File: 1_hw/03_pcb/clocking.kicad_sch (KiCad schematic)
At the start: 0 parts

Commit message: FEAT: Swapped out DDS IC and connected. Started adding Clockign Components into Schematic.
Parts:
- added U?: ADG1219BRJZ, TBD, symbol BRZK_MUX:ADG1219BRJZ
- added X?: ASE-10.000MHz, Oscillator:Oscillator_SMD_Abracon_ASE-4Pin_3.2x2.5mm, symbol Oscillator:ASE-xxxMHz
- added X?: ASE-100.000MHz, Oscillator:Oscillator_SMD_Abracon_ASE-4Pin_3.2x2.5mm, symbol Oscillator:ASE-xxxMHz
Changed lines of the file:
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@@
 		(company "Tomasz Brzyzek")
 	)
+	(symbol
+		(lib_id "Oscillator:ASE-xxxMHz")
+		(at 97.79 72.39 0)
+		(unit 1)
+		(exclude_from_sim no)
+		(in_bom yes)
+		(on_board yes)
+		(dnp no)
+		(property "Reference" "X?"
+			(at 111.76 66.04 0)
+			(effects
+				(font
+					(size 1.27 1.27)
+				)
+			)
+		)
+		(property "Value" "ASE-10.000MHz"
+			(at 111.76 68.58 0)
+			(effects
+				(font
+					(size 1.27 1.27)
+				)
+			)
+		)
+		(property "Footprint" "Oscillator:Oscillator_SMD_Abracon_ASE-4Pin_3.2x2.5mm"
+			(at 115.57 81.28 0)
+			(effects
+				(font
+					(size 1.27 1.27)
+				)
+				(hide yes)
+			)
+		)
+		(property "Datasheet" "http://www.abracon.com/Oscillators/ASV.pdf"
+			(at 95.25 72.39 0)
+			(effects
+				(font
+					(size 1.27 1.27)
+				)
+				(hide yes)
+			)
+		)
+		(property "Description" "3.3V CMOS SMD Crystal Clock Oscillator, Abracon"
+			(at 97.79 72.39 0)
+			(effects
+				(font
+					(size 1.27 1.27)
+				)
+				(hide yes)
+			)
+		)
+		(pin "2"
+		)
+		(pin "3"
+		)
+		(pin "1"
+		)
+		(pin "4"
+		)
+		(instances
+			(project ""
+				(path "/866ef9be-3b01-4288-a6e0-a2357aa17e50/59503b16-13c4-4480-8e22-c5a7043d8844"
+					(reference "X?")
+					(unit 1)
+				)
+			)
+		)
+	)
+	(symbol
+		(lib_id "BRZK_MUX:ADG1219BRJZ")
+		(at 58.42 100.33 0)
+		(mirror y)
+		(unit 1)
+		(exclude_from_sim no)
+		(in_bom yes)
+		(on_board yes)
+		(dnp no)
+		(fields_autoplaced yes)
+		(property "Reference" "U?"
+			(at 40.64 94.0114 0)
+			(effects
+				(font
+					(size 1.27 1.27)
+				)
+			)
+		)
+		(property "Value" "ADG1219BRJZ"
+			(at 40.64 96.5514 0)
+			(effects
+				(font
+					(size 1.27 1.27)
+				)
+			)
+		)
+		(property "Footprint" "TBD"
+			(at 58.42 102.87 0)
+			(effects
+				(font
+					(size 1.27 1.27)
+				)
+				(hide yes)
+			)
+		)
+		(property "Datasheet" "https://www.analog.com/media/en/technical-documentation/data-sheets/ADG1219.pdf"
+			(at 58.42 100.33 0)
+			(effects
+				(font
+					(size 1.27 1.27)
+				)
+				(hide yes)
+			)
+		)
+		(property "Description" "Low Capacitance, Low Charge Injection, ±15 V/12 V iCMOS® SPDT in SOT-23"
+			(at 58.42 100.33 0)
+			(effects
+				(font
+					(size 1.27 1.27)
+				)
+				(hide yes)
+			)
+		)
+		(pin "6"
+		)
+		(pin "5"
+		)
+		(pin "4"
+		)
+		(pin "3"
+		)
+		(pin "8"
+		)
+		(pin "7"
+		)
+		(pin "2"
+		)
+		(pin "1"
+		)
+		(instances
+			(project "arb"
+				(path "/866ef9be-3b01-4288-a6e0-a2357aa17e50/59503b16-13c4-4480-8e22-c5a7043d8844"
+					(reference "U?")
+					(unit 1)
+				)
+			)
+		)
+	)
+	(symbol
+		(lib_id "Oscillator:ASE-xxxMHz")
+		(at 90.17 148.59 0)
+		(unit 1)
+		(exclude_from_sim no)
+		(in_bom yes)
+		(on_board yes)
+		(dnp no)
+		(property "Reference" "X?"
+			(at 104.14 142.24 0)
+			(effects
+				(font
+					(size 1.27 1.27)
+				)
+			)
+		)
+		(property "Value" "ASE-100.000MHz"
+			(at 104.14 144.78 0)
+			(effects
+				(font
+					(size 1.27 1.27)
+				)
+			)
+		)
+		(property "Footprint" "Oscillator:Oscillator_SMD_Abracon_ASE-4Pin_3.2x2.5mm"
+			(at 107.95 157.48 0)
+			(effects
+				(font
+					(size 1.27 1.27)
+				)
+				(hide yes)
+			)
+		)
+		(property "Datasheet" "http://www.abracon.com/Oscillators/ASV.pdf"
+			(at 87.63 148.59 0)
+			(effects
+				(font
+					(size 1.27 1.27)
+				)
+				(hide yes)
+			)
+		)
+		(property "Description" "3.3V CMOS SMD Crystal Clock Oscillator, Abracon"
+			(at 90.17 148.59 0)
+			(effects
+				(font
+					(size 1.27 1.27)
+				)
+				(hide yes)
+			)
+		)
+		(pin "2"
+		)
+		(pin "3"
+		)
+		(pin "1"
+		)
+		(pin "4"
+		)
+		(instances
+			(project "arb"
+				(path "/866ef9be-3b01-4288-a6e0-a2357aa17e50/59503b16-13c4-4480-8e22-c5a7043d8844"
+					(reference "X?")
+					(unit 1)
+				)
+			)
+		)
+	)
 )

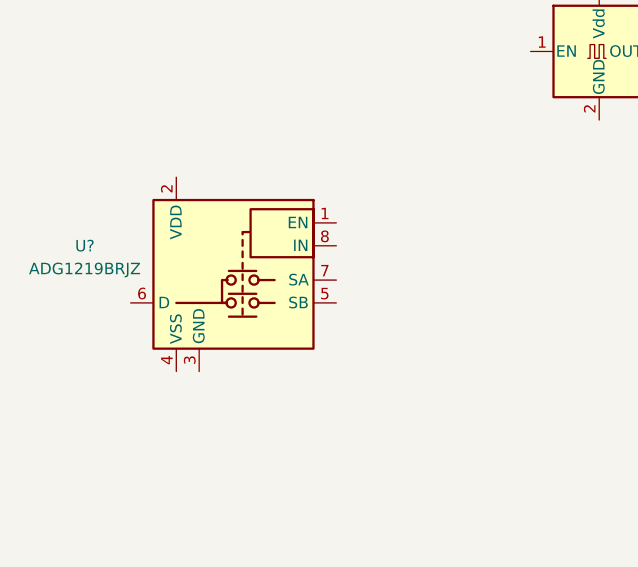
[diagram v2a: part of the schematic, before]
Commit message: FEAT: Added +15V and -15V Regulator. Replaced some Symbols to add additional Part Number Field.
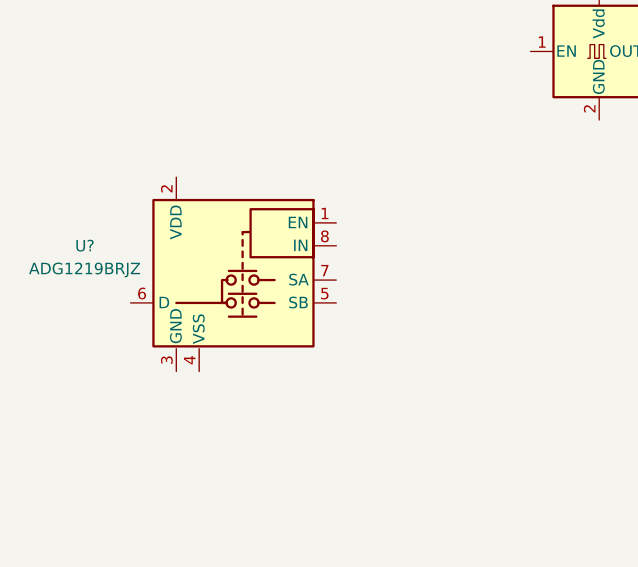
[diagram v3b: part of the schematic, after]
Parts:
- U?: footprint TBD -> BRZK_TBD; Part Number (none) -> ADG1219BRJZ
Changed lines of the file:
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@@
 			)
 		)
-		(property "Footprint" "TBD"
+		(property "Footprint" "BRZK_TBD"
 			(at 58.42 102.87 0)
 			(effects
@@
 			(at 58.42 100.33 0)
 			(effects
+				(font
+					(size 1.27 1.27)
+				)
+				(hide yes)
+			)
+		)
+		(property "Part Number" "ADG1219BRJZ"
+			(at 58.42 100.33 0)
+			(effects

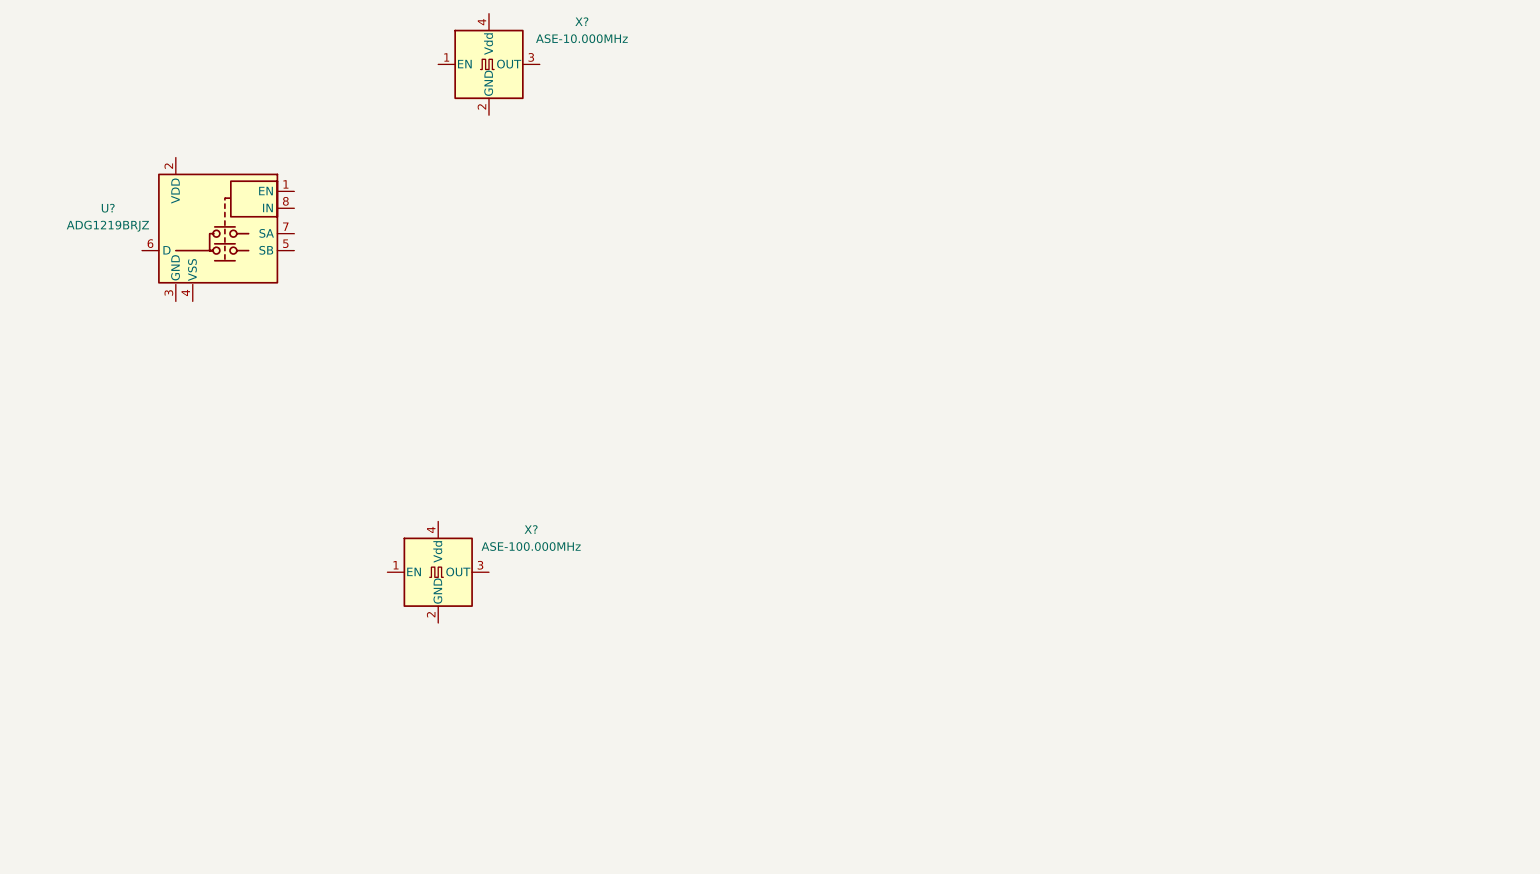
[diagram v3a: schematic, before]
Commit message: FEAT: Added Clocking Sheet, FPGA Flash, and FPGA Decoupling.
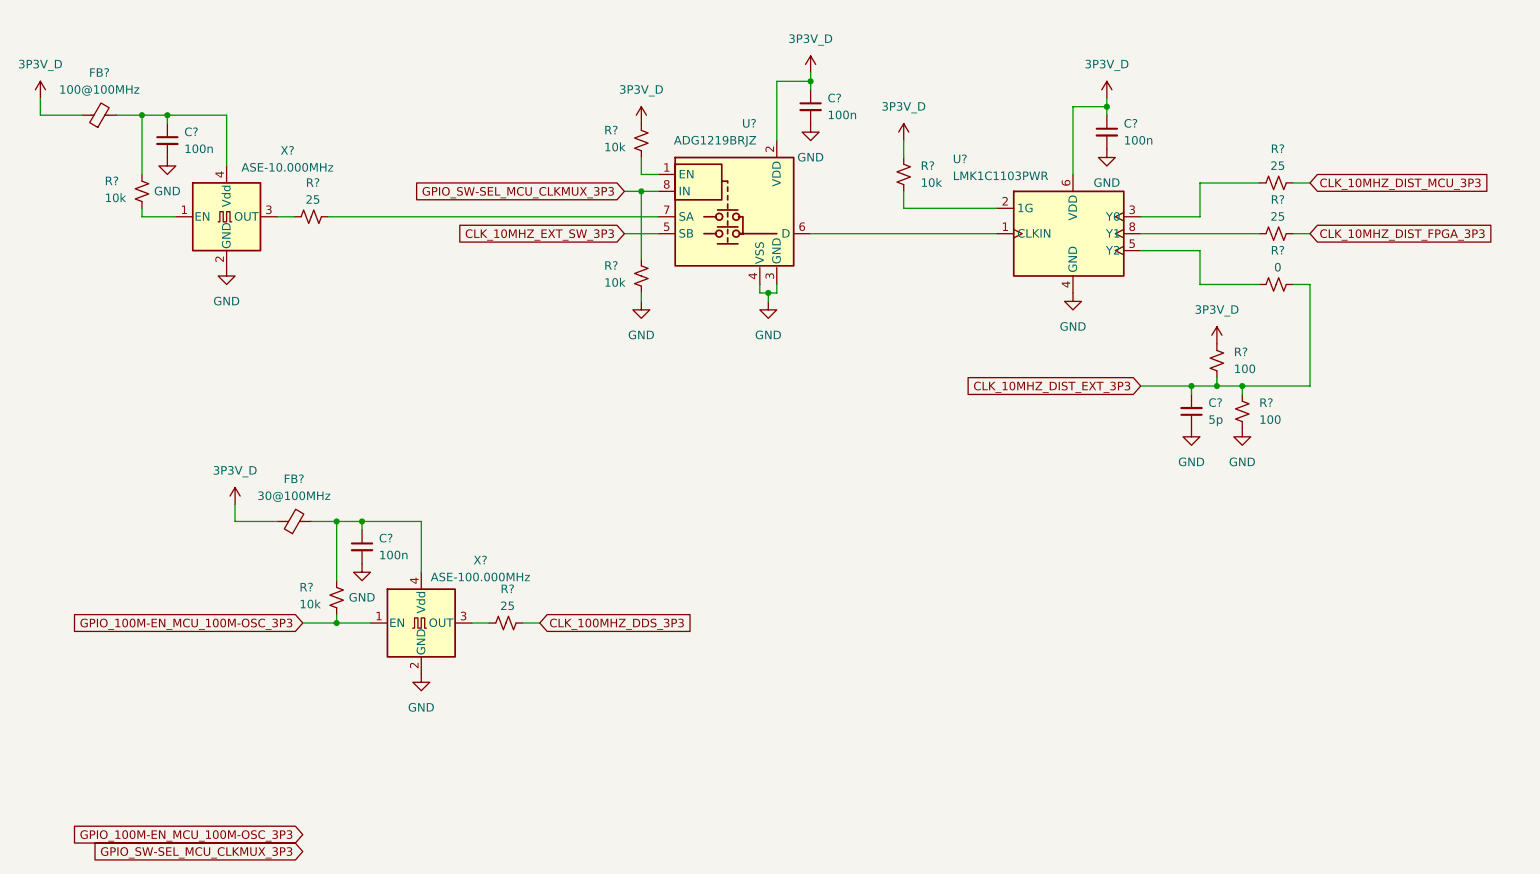
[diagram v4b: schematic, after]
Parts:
- removed X?: ASE-100.000MHz, Oscillator:Oscillator_SMD_Abracon_ASE-4Pin_3.2x2.5mm, symbol Oscillator:ASE-xxxMHz
- added C? (x4): 100n, Capacitor_SMD:C_0603_1608Metric, symbol Device:C_Small
- added C?: 5p, symbol Device:C_Small
- added FB?: 100@100MHz, symbol Device:FerriteBead_Small
- added FB?: 30@100MHz, symbol Device:FerriteBead_Small
- added R? (x4): 25, Resistor_SMD:R_0603_1608Metric, symbol Device:R_Small_US
- added R? (x5): 10k, Resistor_SMD:R_0603_1608Metric, symbol Device:R_Small_US
- added R? (x2): 100, symbol Device:R_Small_US
- added R?: 0, Resistor_SMD:R_0603_1608Metric, symbol Device:R_Small_US
- added U?: LMK1C1103PWR, Package_SO:TSSOP-8_4.4x3mm_P0.65mm, symbol BRZK_CLOCK:LMK1C1103PWR
- added X?: ASE-100.000MHz, Oscillator:Oscillator_SMD_Abracon_ASE-4Pin_3.2x2.5mm, symbol Oscillator:ASE-xxxMHz
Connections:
- net at X?.1 (EN): now also R?.1
- net GND: now reaches X?.2 (GND)
- net GND: now also U?.3 (GND), U?.4 (VSS), C?.1, C?.2, C?.2, C?.2, C?.2, R?.1, R?.1, U?.4 (GND), X?.2 (GND)
- net at X?.3 (OUT): now also R?.2
- net at X?.4 (Vdd): now also C?.1, FB?.2, R?.2
- net at U?.1 (EN): now also R?.1
- net 3P3V_D: now reaches U?.2 (VDD)
- net 3P3V_D: now also C?.1, C?.1, FB?.1, FB?.1, R?.2, R?.2, R?.2, U?.6 (VDD)
- net CLK_10MHZ_EXT_SW_3P3: now reaches U?.5 (SB)
- net at U?.6 (D): now also U?.1 (CLKIN)
- net at U?.7 (SA): now also R?.1
- net GPIO_SW-SEL_MCU_CLKMUX_3P3: now reaches U?.8 (IN)
- net GPIO_SW-SEL_MCU_CLKMUX_3P3: now also R?.2
- new net: R?.2, U?.8 (Y1)
- new net: R?.1, U?.2 (1G)
- new net: C?.1, FB?.2, R?.2, X?.4 (Vdd)
- new net: R?.2, X?.3 (OUT)
- new net: R?.2, U?.5 (Y2)
- new net: R?.2, U?.3 (Y0)
- new net CLK_100MHZ_DDS_3P3: R?.1
- new net CLK_10MHZ_DIST_EXT_3P3: C?.2, R?.1, R?.1, R?.2
- new net CLK_10MHZ_DIST_FPGA_3P3: R?.1
- new net CLK_10MHZ_DIST_MCU_3P3: R?.1
- new net GPIO_100M-EN_MCU_100M-OSC_3P3: R?.1, X?.1 (EN)
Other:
- moved on the sheet: U?, X?

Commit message: FEAT: Added Connectors on Schematic. Created Connector Footprints.
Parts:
- gave numbers to parts that had none: 23
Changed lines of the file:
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@@
 		(on_board yes)
 		(dnp no)
-		(property "Reference" "R?"
+		(property "Reference" "R38"
 			(at 216.154 92.71 90)
 			(effects
@@
 			(project "arb"
 				(path "/866ef9be-3b01-4288-a6e0-a2357aa17e50/59503b16-13c4-4480-8e22-c5a7043d8844"
-					(reference "R?")
+					(reference "R38")
 					(unit 1)
 				)
@@
 		(dnp no)
 		(fields_autoplaced yes)
-		(property "Reference" "C?"
+		(property "Reference" "C69"
 			(at 52.07 82.5563 0)
 			(effects
@@
 			(project "arb"
 				(path "/866ef9be-3b01-4288-a6e0-a2357aa17e50/59503b16-13c4-4480-8e22-c5a7043d8844"
-					(reference "C?")
+					(reference "C69")
 					(unit 1)
 				)
@@
 		(on_board yes)
 		(dnp no)
-		(property "Reference" "R?"
+		(property "Reference" "R33"
 			(at 115.062 102.616 0)
 			(effects
@@
 			(project "arb"
 				(path "/866ef9be-3b01-4288-a6e0-a2357aa17e50/59503b16-13c4-4480-8e22-c5a7043d8844"
-					(reference "R?")
+					(reference "R33")
 					(unit 1)
 				)
@@
 		(on_board yes)
 		(dnp no)
-		(property "Reference" "R?"
+		(property "Reference" "R29"
 			(at 71.374 90.17 90)
 			(effects
@@
 			(project "arb"
 				(path "/866ef9be-3b01-4288-a6e0-a2357aa17e50/59503b16-13c4-4480-8e22-c5a7043d8844"
-					(reference "R?")
+					(reference "R29")
 					(unit 1)
 				)
@@
 		(on_board yes)
 		(dnp no)
-		(property "Reference" "X?"
+		(property "Reference" "X1"
 			(at 67.564 85.344 0)
 			(effects
@@
 			(project ""
 				(path "/866ef9be-3b01-4288-a6e0-a2357aa17e50/59503b16-13c4-4480-8e22-c5a7043d8844"
-					(reference "X?")
+					(reference "X1")
 					(unit 1)
 				)
@@
 		(on_board yes)
 		(dnp no)
-		(property "Reference" "U?"
+		(property "Reference" "U12"
 			(at 137.9535 81.28 0)
 			(effects
@@
 			(project "arb"
 				(path "/866ef9be-3b01-4288-a6e0-a2357aa17e50/59503b16-13c4-4480-8e22-c5a7043d8844"
-					(reference "U?")
+					(reference "U12")
 					(unit 1)
 				)
@@
 		(dnp no)
 		(fields_autoplaced yes)
-		(property "Reference" "R?"
+		(property "Reference" "R36"
 			(at 213.36 123.1899 0)
 			(effects
@@
 			(project "arb"
 				(path "/866ef9be-3b01-4288-a6e0-a2357aa17e50/59503b16-13c4-4480-8e22-c5a7043d8844"
-					(reference "R?")
+					(reference "R36")
 					(unit 1)
 				)
@@
 		(dnp no)
 		(fields_autoplaced yes)
-		(property "Reference" "C?"
+		(property "Reference" "C73"
 			(at 205.74 123.1835 0)
 			(effects
@@
 			(project "arb"
 				(path "/866ef9be-3b01-4288-a6e0-a2357aa17e50/59503b16-13c4-4480-8e22-c5a7043d8844"
-					(reference "C?")
+					(reference "C73")
 					(unit 1)
 				)
@@
 		(dnp no)
 		(fields_autoplaced yes)
-		(property "Reference" "R?"
+		(property "Reference" "R34"
 			(at 162.56 87.6299 0)
 			(effects
@@
 			(project "arb"
 				(path "/866ef9be-3b01-4288-a6e0-a2357aa17e50/59503b16-13c4-4480-8e22-c5a7043d8844"
-					(reference "R?")
+					(reference "R34")
 					(unit 1)
 				)
@@
 		(dnp no)
 		(fields_autoplaced yes)
-		(property "Reference" "C?"
+		(property "Reference" "C70"
 			(at 81.28 143.5163 0)
 			(effects
@@
 			(project "arb"
 				(path "/866ef9be-3b01-4288-a6e0-a2357aa17e50/59503b16-13c4-4480-8e22-c5a7043d8844"
-					(reference "C?")
+					(reference "C70")
 					(unit 1)
 				)
@@
 		(on_board yes)
 		(dnp no)
-		(property "Reference" "R?"
+		(property "Reference" "R30"
 			(at 69.342 150.876 0)
 			(effects
@@
 			(project "arb"
 				(path "/866ef9be-3b01-4288-a6e0-a2357aa17e50/59503b16-13c4-4480-8e22-c5a7043d8844"
-					(reference "R?")
+					(reference "R30")
 					(unit 1)
 				)
@@
 		(on_board yes)
 		(dnp no)
-		(property "Reference" "R?"
+		(property "Reference" "R31"
 			(at 100.584 151.13 90)
 			(effects
@@
 			(project "arb"
 				(path "/866ef9be-3b01-4288-a6e0-a2357aa17e50/59503b16-13c4-4480-8e22-c5a7043d8844"
-					(reference "R?")
+					(reference "R31")
 					(unit 1)
 				)
@@
 		(on_board yes)
 		(dnp no)
-		(property "Reference" "R?"
+		(property "Reference" "R39"
 			(at 216.154 100.33 90)
 			(effects
@@
 			(project "arb"
 				(path "/866ef9be-3b01-4288-a6e0-a2357aa17e50/59503b16-13c4-4480-8e22-c5a7043d8844"
-					(reference "R?")
+					(reference "R39")
 					(unit 1)
 				)
@@
 		(on_board yes)
 		(dnp no)
-		(property "Reference" "R?"
+		(property "Reference" "R32"
 			(at 115.062 82.296 0)
 			(effects
@@
 			(project "arb"
 				(path "/866ef9be-3b01-4288-a6e0-a2357aa17e50/59503b16-13c4-4480-8e22-c5a7043d8844"
-					(reference "R?")
+					(reference "R32")
 					(unit 1)
 				)
@@
 		(dnp no)
 		(fields_autoplaced yes)
-		(property "Reference" "FB?"
+		(property "Reference" "FB1"
 			(at 39.3319 73.66 90)
 			(effects
@@
 			(project ""
 				(path "/866ef9be-3b01-4288-a6e0-a2357aa17e50/59503b16-13c4-4480-8e22-c5a7043d8844"
-					(reference "FB?")
+					(reference "FB1")
 					(unit 1)
 				)
@@
 		(on_board yes)
 		(dnp no)
-		(property "Reference" "R?"
+		(property "Reference" "R28"
 			(at 40.132 89.916 0)
 			(effects
@@
 			(project "arb"
 				(path "/866ef9be-3b01-4288-a6e0-a2357aa17e50/59503b16-13c4-4480-8e22-c5a7043d8844"
-					(reference "R?")
+					(reference "R28")
 					(unit 1)
 				)
@@
 		(on_board yes)
 		(dnp no)
-		(property "Reference" "R?"
+		(property "Reference" "R37"
 			(at 216.154 85.09 90)
 			(effects
@@
 			(project "arb"
 				(path "/866ef9be-3b01-4288-a6e0-a2357aa17e50/59503b16-13c4-4480-8e22-c5a7043d8844"
-					(reference "R?")
+					(reference "R37")
 					(unit 1)
 				)
@@
 		(dnp no)
 		(fields_autoplaced yes)
-		(property "Reference" "C?"
+		(property "Reference" "C71"
 			(at 148.59 77.4763 0)
 			(effects
@@
 			(project "arb"
 				(path "/866ef9be-3b01-4288-a6e0-a2357aa17e50/59503b16-13c4-4480-8e22-c5a7043d8844"
-					(reference "C?")
+					(reference "C71")
 					(unit 1)
 				)
@@
 		(dnp no)
 		(fields_autoplaced yes)
-		(property "Reference" "FB?"
+		(property "Reference" "FB2"
 			(at 68.5419 134.62 90)
 			(effects
@@
 			(project "arb"
 				(path "/866ef9be-3b01-4288-a6e0-a2357aa17e50/59503b16-13c4-4480-8e22-c5a7043d8844"
-					(reference "FB?")
+					(reference "FB2")
 					(unit 1)
 				)
@@
 		(dnp no)
 		(fields_autoplaced yes)
-		(property "Reference" "R?"
+		(property "Reference" "R35"
 			(at 209.55 115.5699 0)
 			(effects
@@
 			(project "arb"
 				(path "/866ef9be-3b01-4288-a6e0-a2357aa17e50/59503b16-13c4-4480-8e22-c5a7043d8844"
-					(reference "R?")
+					(reference "R35")
 					(unit 1)
 				)
@@
 		(dnp no)
 		(fields_autoplaced yes)
-		(property "Reference" "C?"
+		(property "Reference" "C72"
 			(at 193.04 81.2863 0)
 			(effects
@@
 			(project "arb"
 				(path "/866ef9be-3b01-4288-a6e0-a2357aa17e50/59503b16-13c4-4480-8e22-c5a7043d8844"
-					(reference "C?")
+					(reference "C72")
 					(unit 1)
 				)
@@
 		(on_board yes)
 		(dnp no)
-		(property "Reference" "X?"
+		(property "Reference" "X2"
 			(at 96.52 146.812 0)
 			(effects
@@
 			(project "arb"
 				(path "/866ef9be-3b01-4288-a6e0-a2357aa17e50/59503b16-13c4-4480-8e22-c5a7043d8844"
-					(reference "X?")
+					(reference "X2")
 					(unit 1)
 				)
@@
 		(on_board yes)
 		(dnp no)
-		(property "Reference" "U?"
+		(property "Reference" "U13"
 			(at 167.386 86.614 0)
 			(effects
@@
 			(project ""
 				(path "/866ef9be-3b01-4288-a6e0-a2357aa17e50/59503b16-13c4-4480-8e22-c5a7043d8844"
-					(reference "U?")
-					(unit 1)
-				)
+					(reference "U13")
+					(unit 1)
+				)
